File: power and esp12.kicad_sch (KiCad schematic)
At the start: 14 parts, among them P2 USB_C_Plug_USB2.0, Q1 S8050, Q2 S8050, U5 CH340C

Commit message: add: protector de estatica
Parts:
- removed C9: 0.1uf, Capacitor_SMD:C_1206_3216Metric, symbol Device:C
- removed D1, D2, D3, D4: LESD5D5.0CT1G, Diode_SMD:Nexperia_DSN1608-2_1.6x0.8mm, symbol Diode:PTVS5V0Z1USK
- added D1: BAT60A, SparkFun-Semiconductor-Standard:SOD-323, symbol SparkFun-DiscreteSemi:D_Schottky_3A_10V_0.28V
- added R7: 5.1k, Resistor_SMD:R_1206_3216Metric, symbol Device:R_US
- added U4: DT1042-04SO, SparkFun-Semiconductor-Standard:SOT23-6, symbol SparkFun-DiscreteSemi:D_TVS_ESD_USB
- Q1, Q2: footprint Package_TO_SOT_THT:TO-92_Inline -> Package_TO_SOT_SMD:SOT-23
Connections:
- net GND: now also R7.1, U4.2 (GND)
- net usb_5v: now also D1.C
- net at P2.A6 (D+), R4.1: now also U4.6 (I/O4)
- net at P2.A4 (VBUS), P2.A9 (VBUS), P2.B4 (VBUS)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: now also D1.A, U4.5 (VCC)
- net at P2.A7 (D-), R3.1: now also U4.4 (I/O3)
- net at P2.B5 (VCONN): now also R7.2
- net esp_rst renamed EN
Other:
- moved on the sheet: R5

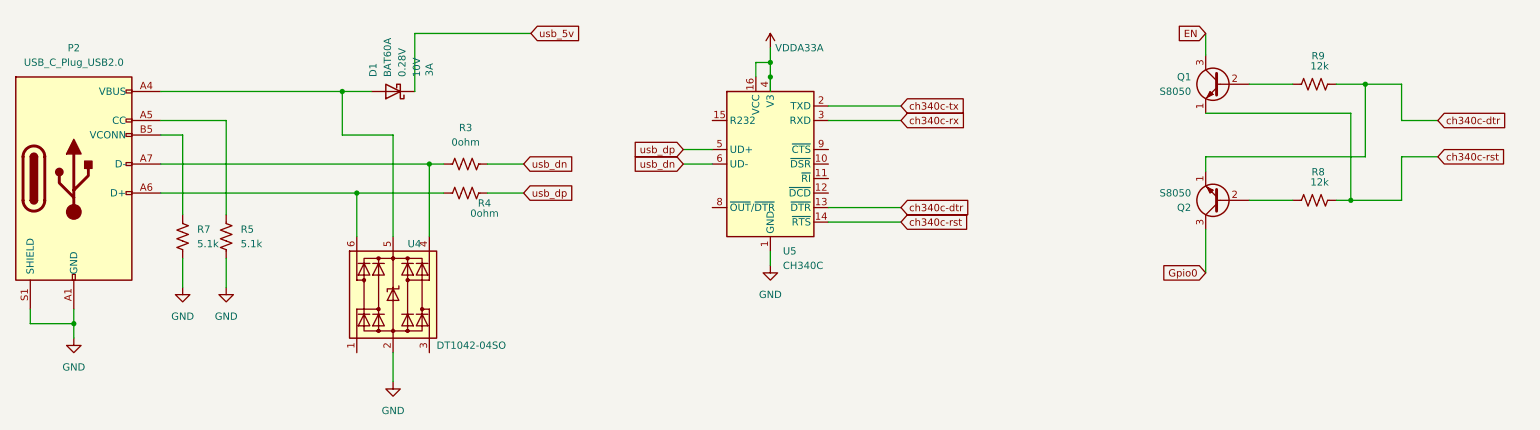
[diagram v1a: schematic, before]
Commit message: del: elimine el ch340 y conecte el usb directamente
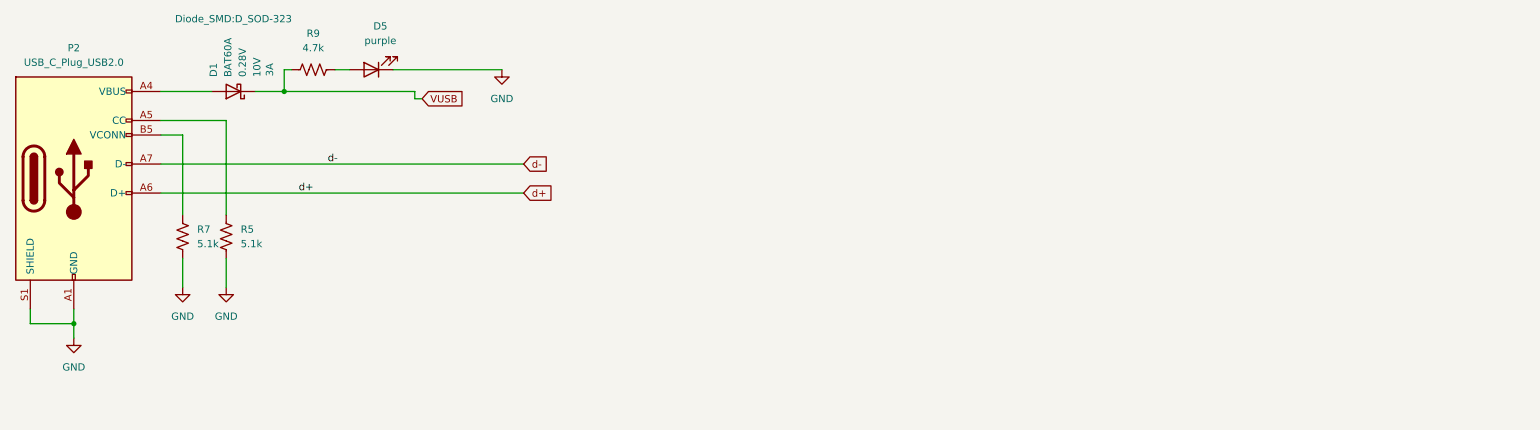
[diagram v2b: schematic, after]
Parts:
- removed Q1, Q2: S8050, Package_TO_SOT_SMD:SOT-23, symbol Transistor_BJT:S8050
- removed R3, R4: 0ohm, Resistor_SMD:R_1206_3216Metric, symbol Device:R_US
- removed R8, R9: 12k, Resistor_SMD:R_1206_3216Metric, symbol Device:R_US
- removed U4: DT1042-04SO, SparkFun-Semiconductor-Standard:SOT23-6, symbol SparkFun-DiscreteSemi:D_TVS_ESD_USB
- removed U5: CH340C, Package_SO:SOIC-16_3.9x9.9mm_P1.27mm, symbol Interface_USB:CH340C
- added D5: purple, LED_SMD:LED_0603_1608Metric, symbol SparkFun-LED:LED_Red_0603
- added R9: 4.7k, Resistor_SMD:R_0402_1005Metric, symbol SparkFun-Resistor:4.7k_0402
- D1: footprint SparkFun-Semiconductor-Standard:SOD-323 -> Diode_SMD:D_SOD-323
- R5, R7: footprint Resistor_SMD:R_1206_3216Metric -> Resistor_SMD:R_0402_1005Metric
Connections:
- net GND: now also D5.1 (K)
- net d+: now reaches P2.A6 (D+)
- net at P2.A4 (VBUS), P2.A9 (VBUS), P2.B4 (VBUS)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: now also D1.1; no longer D1.A
- net d-: now reaches P2.A7 (D-)
- removed net usb_5v: D1.C
- new net: D5.2 (A), R9.2
- new net VUSB: D1.2, R9.1
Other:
- moved on the sheet: D1
